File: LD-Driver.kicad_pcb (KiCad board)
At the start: 2 copper layers, 99 x 80 mm, 131 parts, among them J1 BASYS3, J2 Conn_02x07_Counter_Clockwise, J3 Barrel_Jack_Switch, Q1 RJK0355DSP, Q10 RJK0355DSP, Q2 RJK0355DSP, Q3 SiRC18DP, Q4 SiRC18DP, Q5 SiRC18DP, Q6 SiRC18DP, Q7 DMP3037LSS-13, Q8 2N7002, Q9 RJK0355DSP, U1 MCP4728, U2 LT3743, U3 MAX1978, U4 INA333xxDGK, U5 MIC2101

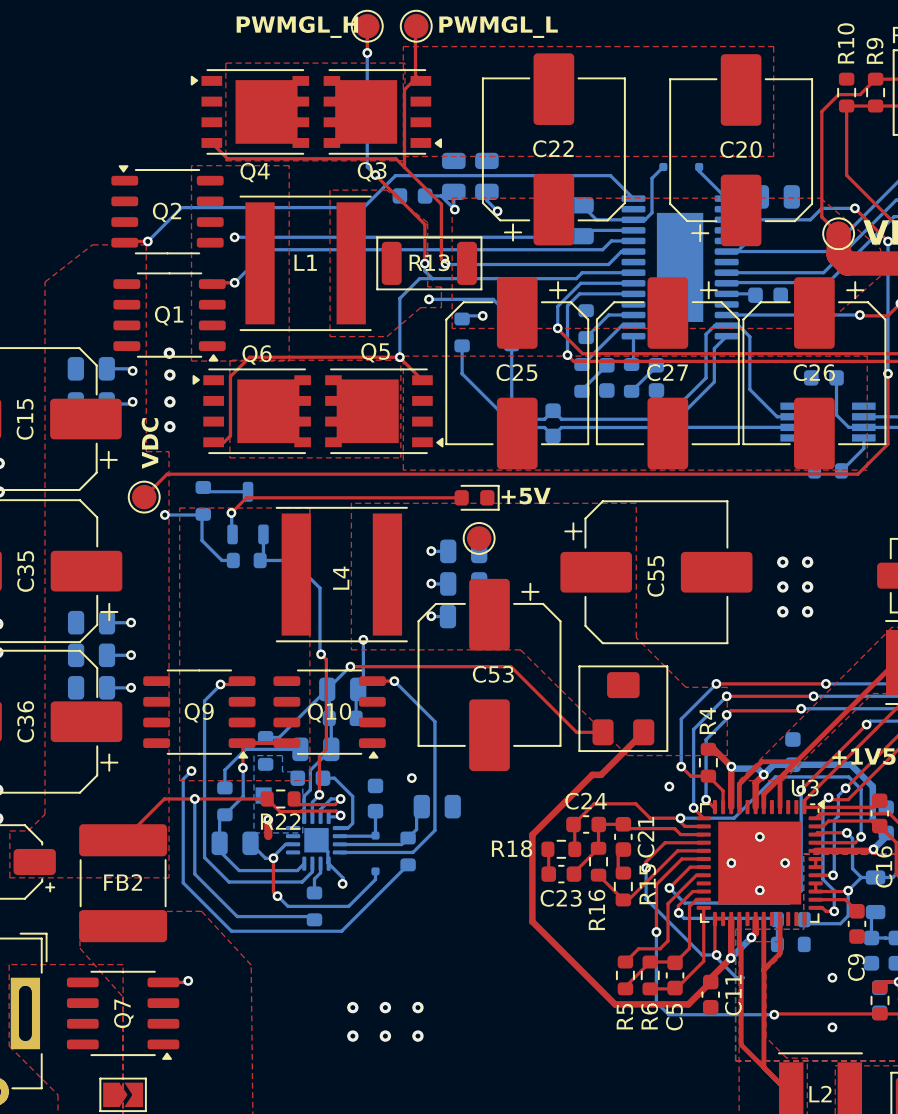
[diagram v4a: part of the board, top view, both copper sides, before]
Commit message: small corrections to PCB, fixed some capacitors' voltage ratings and footprints to make BOM more uniform
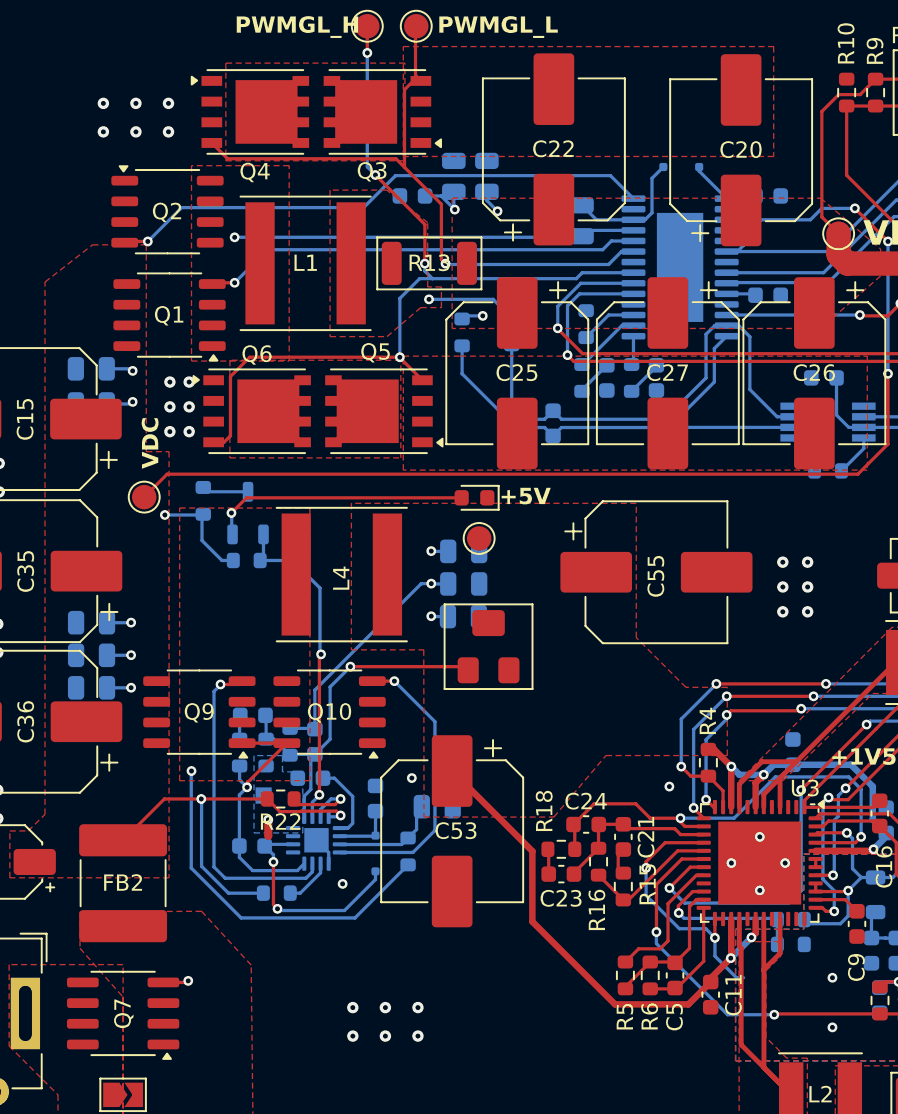
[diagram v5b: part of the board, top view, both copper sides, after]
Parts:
- C44, C45, C46, C8: footprint Capacitor_SMD:C_0805_2012Metric -> Capacitor_SMD:C_0603_1608Metric
- moved C53 9.87 mm to (99.2, 104.8)
- moved RV2 9.11 mm to (101.4, 93.5)
- moved C45 4.40 mm to (87.0, 97.7)
- moved C46 3.64 mm to (90.8, 99.3), turned to 90 degrees
- moved R26 3.54 mm to (89.3, 99.3), turned to 90 degrees
- moved R25 3.13 mm to (86.2, 100.0)
- moved R23 2.45 mm to (88.4, 108.6), turned to 180 degrees
- moved C44 1.05 mm to (86.9, 105.7)
- moved C8 0.51 mm to (118.6, 65.8)
- moved R27 0.10 mm to (87.8, 100.0)
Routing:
- net /Power/FB: track 32.8 -> 22.6 mm
- net +5V: track 72.3 -> 77.7 mm, vias 9 -> 8
- net Net-(C45-Pad2): track 6.26 -> 1.48 mm
- net VDC: track 113.4 -> 108.9 mm
- net Net-(U5-SW): track 41.5 -> 38.0 mm
- net /Driver/NTC+: track 45.9 -> 43.8 mm
- net GND: track 4.92 -> 3.31 mm, vias 46 -> 54
- net Net-(U5-FREQ): track 1.96 -> 2.94 mm
- net GNDA: track 17.7 -> 17.0 mm
- net /Power/DH: track 20.5 -> 19.8 mm

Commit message: small fixes to PCB and silkscreen
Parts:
- moved R21 8.72 mm to (95.3, 87.6)
- moved Q8 8.72 mm to (95.4, 84.7)
- moved R20 8.72 mm to (92.6, 84.0)
- moved C55 4.32 mm to (111.6, 93.2)
- moved D2 3.22 mm to (103.8, 84.5)
- moved TP14 3.22 mm to (104.1, 87.0)
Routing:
- net Net-(D2-A): track 15.9 -> 9.35 mm
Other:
- board text added: "P_GOOD"

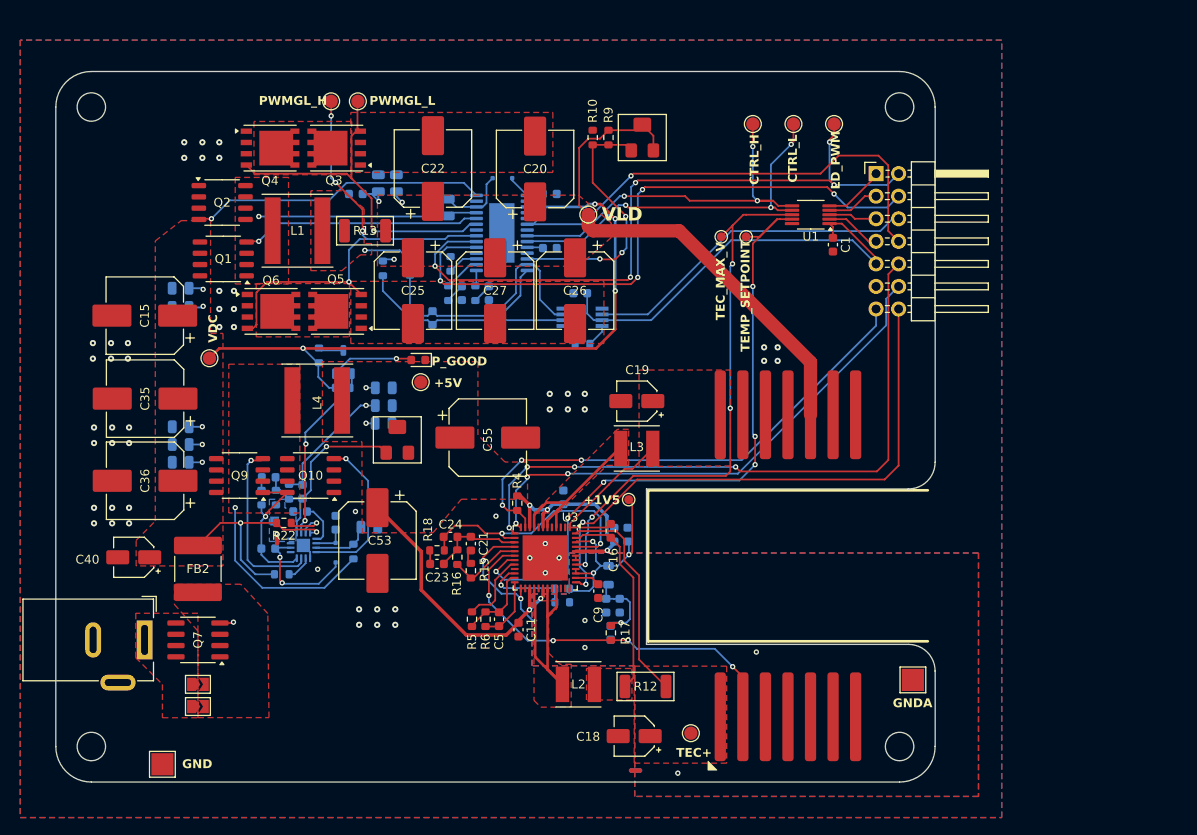
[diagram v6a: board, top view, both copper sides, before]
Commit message: feat: made possible to swap butterfly pins for compatibility
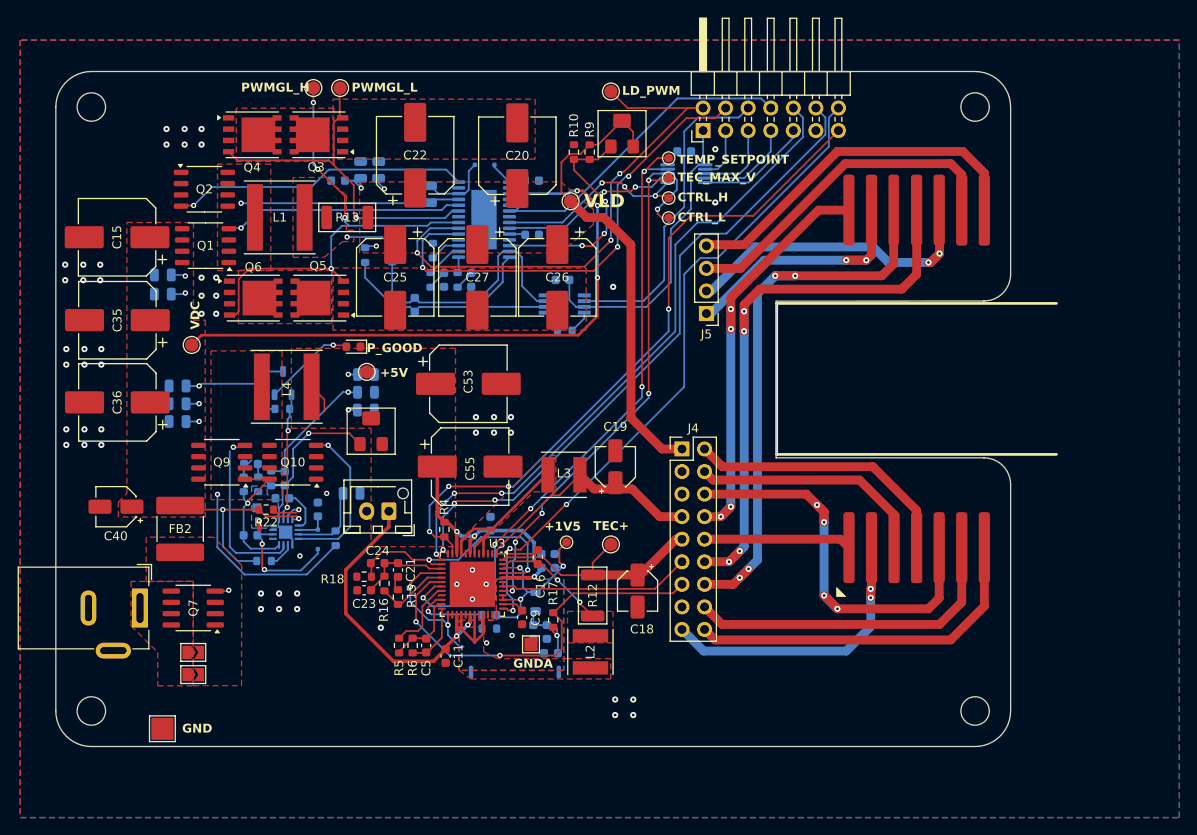
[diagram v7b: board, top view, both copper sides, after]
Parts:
- added J4: SELECTOR, Connector_PinHeader_2.54mm:PinHeader_2x09_P2.54mm_Vertical, F.Cu at (133.5, 94.5)
- added J5: Conn_02x07_Counter_Clockwise, Connector_PinHeader_2.54mm:PinHeader_1x04_P2.54mm_Vertical, F.Cu at (136.2, 79.2)
- added J6: Conn_01x02, Connector_JST:JST_XH_B2B-XH-AM_1x02_P2.50mm_Vertical, F.Cu at (100.5, 101.5)
- C1, NT1, U1: moved to B.Cu
- J2: value Conn_02x07_Counter_Clockwise -> BUTTERFLY
- TP2: footprint TestPoint:TestPoint_Pad_2.5x2.5mm -> TestPoint:TestPoint_Pad_1.5x1.5mm
- TP8, TP9: footprint TestPoint:TestPoint_Pad_D1.5mm -> TestPoint:TestPoint_Pad_D1.0mm
- moved TP2 43.2 mm to (116.5, 116.5)
- moved J2 25.5 mm to (159.9, 86.6)
- moved TP7 25.4 mm to (125.5, 54.2), turned to -90 degrees
- moved TP3 23.1 mm to (125.5, 105.2)
- moved NT1 21.6 mm to (109.8, 119.6), turned to 90 degrees
- moved C53 20.4 mm to (109.4, 87.2), turned to 0 degrees
- moved J1 20.1 mm to (135.9, 58.6), turned to 90 degrees
- moved C1 19.8 mm to (133.8, 61.0), turned to 180 degrees
- moved TP9 17.6 mm to (132.0, 68.5), turned to -90 degrees
- moved C18 16.3 mm to (128.5, 110.5), turned to -90 degrees
- moved U1 14.7 mm to (134.0, 63.5)
- moved NT3 14.0 mm to (119.6, 119.6), turned to 90 degrees
- moved TP8 12.6 mm to (132.0, 66.2)
- moved TP11 12.4 mm to (132.0, 61.8), turned to -90 degrees
- moved R12 11.8 mm to (123.4, 111.0), turned to 90 degrees
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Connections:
- J1 pad 1: /RDY/~{BSY} -> +3V3
- J1 pad 3: /~{LDAC} -> /SCL
- J1 pad 7: /SCL -> /~{LDAC}
- J1 pad 9: +3V3 -> /RDY/~{BSY}
- J2 pad 1: /Driver/TEC+ -> /Driver/Pin_1
- J2 pad 10: /Driver/LD -> /Driver/Pin_10
- J2 pad 11: GND -> /Driver/Pin_11
- J2 pad 12: unconnected-(J2-Pin_12-Pad12) -> /Driver/Pin_12
- J2 pad 13: unconnected-(J2-Pin_13-Pad13) -> /Driver/Pin_13
- J2 pad 14: /Driver/TEC- -> /Driver/Pin_14
- J2 pad 2: /Driver/NTC+ -> /Driver/Pin_2
- J2 pad 3: unconnected-(J2-Pin_3-Pad3) -> /Driver/Pin_3
- J2 pad 4: unconnected-(J2-Pin_4-Pad4) -> /Driver/Pin_4
- J2 pad 5: GNDA -> /Driver/Pin_5
- J2 pad 6: unconnected-(J2-Pin_6-Pad6) -> /Driver/Pin_6
- J2 pad 7: unconnected-(J2-Pin_7-Pad7) -> /Driver/Pin_7
- J2 pad 8: unconnected-(J2-Pin_8-Pad8) -> /Driver/Pin_8
- J2 pad 9: unconnected-(J2-Pin_9-Pad9) -> /Driver/Pin_9
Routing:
- net /Driver/Pin_11: track 0.00 -> 64.4 mm, vias 0 -> 4
- net /Driver/Pin_12: track 0.00 -> 63.5 mm, vias 0 -> 4
- net /Driver/Pin_14: track 0.00 -> 48.2 mm, vias 0 -> 4
- net /Driver/Pin_5: track 0.00 -> 47.9 mm, vias 0 -> 4
- net /Driver/Pin_8: track 0.00 -> 40.9 mm
- net /Driver/Pin_7: track 0.00 -> 40.2 mm
- net /Driver/Pin_9: track 0.00 -> 38.1 mm
- net /Driver/Pin_6: track 0.00 -> 37.0 mm
- net /Driver/Pin_10: track 0.00 -> 36.0 mm, vias 0 -> 2
- net /Driver/Pin_2: track 0.00 -> 33.3 mm, vias 0 -> 2
- net /Driver/Pin_4: track 0.00 -> 30.9 mm
- net /Driver/Pin_13: track 0.00 -> 28.6 mm, vias 0 -> 2
- net /Driver/Pin_3: track 0.00 -> 27.1 mm
- net GNDA: track 17.0 -> 38.6 mm, vias 6 -> 4
- net /Driver/CTRL_H_DAC: track 42.7 -> 22.7 mm
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- removed copper zone on F.Cu, net /Driver/TEC+
- removed copper zone on F.Cu, net /Driver/TEC-
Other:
- board size 99 x 80 mm -> 107.5 x 76 mm

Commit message: feat: added method to swap butterfly socket pins to adapt to multiple SOA SNs. Fixed routing imperfections and addes informative silkscreen
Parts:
- moved TP7 6.25 mm to (131.8, 54.2)
- moved TP12 4.12 mm to (76.0, 122.0)
- moved H2 4.00 mm to (67.0, 120.0)
- moved H3 4.00 mm to (166.5, 120.0)
- moved R9 2.91 mm to (121.5, 63.5), turned to -90 degrees
- moved J3 2.41 mm to (72.5, 110.0)
- moved RV1 1.75 mm to (125.0, 59.0)
- moved JP1 1.66 mm to (78.5, 118.2)
- moved JP2 1.66 mm to (78.5, 115.8)
- moved Q7 1.16 mm to (78.5, 111.2)
- moved D2 1.00 mm to (95.5, 83.0)
- moved Q9 1.00 mm to (81.8, 95.0)
- moved C2 0.96 mm to (117.5, 70.0)
- moved FB2 0.79 mm to (77.2, 102.8)
- moved R10 0.60 mm to (121.5, 60.5)
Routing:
- net /LD_MOD: track 61.8 -> 55.5 mm
- net +5V: track 87.5 -> 84.2 mm
- net /Driver/Pin_12: track 63.5 -> 60.5 mm, vias 4 -> 2
- net /Driver/Pin_11: track 64.4 -> 61.5 mm, vias 4 -> 2
- net VDC: track 109.5 -> 112.2 mm
- net Net-(U5-SW): track 38.0 -> 40.3 mm
- net /Driver/Pin_14: track 48.2 -> 46.0 mm, vias 4 -> 2
- net /TEC_EN: track 76.8 -> 74.9 mm
- net /Driver/LD: track 58.6 -> 56.8 mm
- net Net-(C23-Pad1): track 0.00 -> 1.54 mm
- net /Power/DH: track 19.2 -> 20.6 mm
- net Net-(U2-FB): track 26.0 -> 24.7 mm, vias 3 -> 1
- net Net-(D2-A): track 10.6 -> 9.47 mm
- net Net-(U2-SS): track 1.80 -> 2.77 mm
- net Net-(C45-Pad2): track 2.07 -> 1.48 mm
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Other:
- board size 107.5 x 76 mm -> 107.5 x 72 mm
- board text added: "+VLD GND GND TEC- TEC+ NTC- NTC+ NC 2"
- board text added: "- +5V"
- board text added: "1 2 3 4"
- board text added: "11 10"
- board text added: "14 13 12"
- board text added: "4 3 5 14 1 11 12 6 7"
- board text added: "5 6 7"
- board text added: "8 9 10 13"
- board text added: "9 8"
- board text added: "Mirco Tollardo Università di Trento"
- board text added: "RED BOOT INPUT"
